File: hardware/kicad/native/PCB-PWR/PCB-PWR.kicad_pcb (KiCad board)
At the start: 4 copper layers, 90 x 60 mm, 60 parts, among them J1 43045-0213, J2 43045-1202, Q1 CSD18540Q5B, U1 LM74700QDBVRQ1, U2 INA226AIDGSR, U3 LMR604403SRAKR, U4 LMR604403SRAKR, U5 TPS7A2018PDBVR

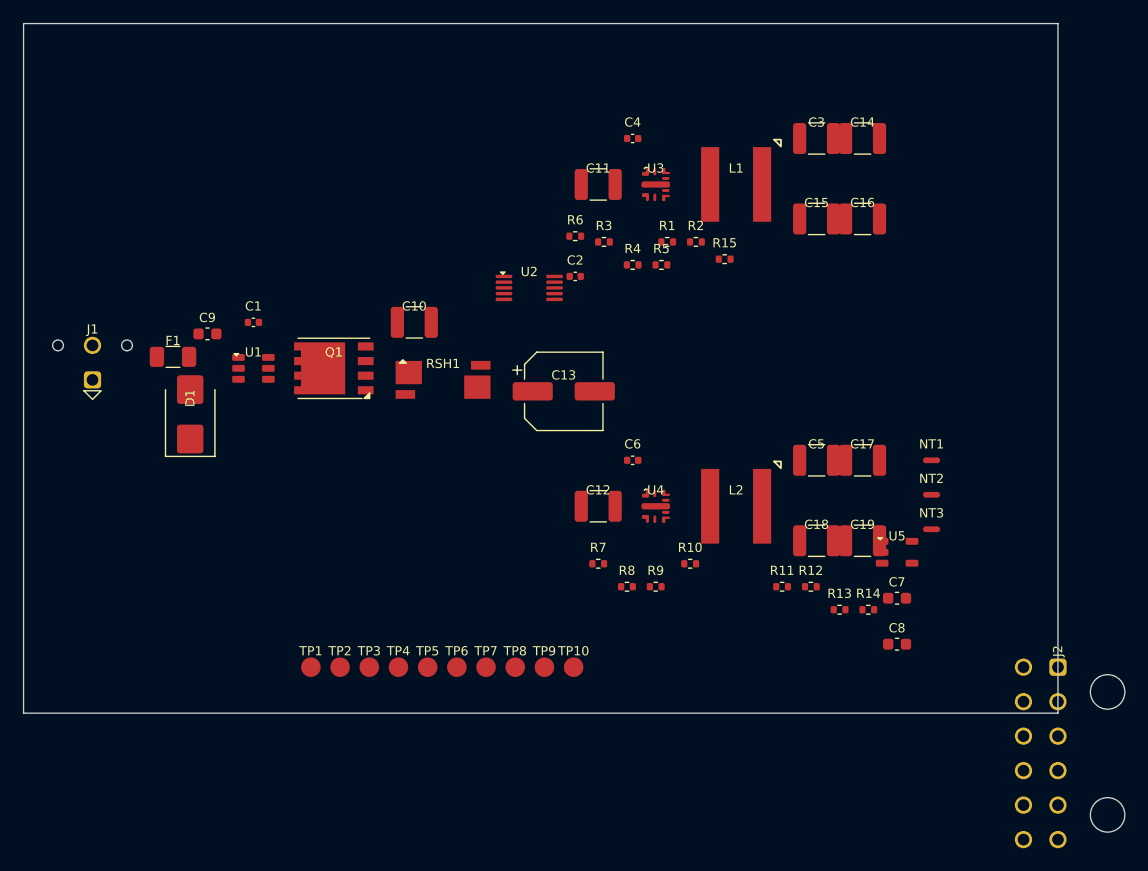
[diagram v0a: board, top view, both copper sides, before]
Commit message: hardware: close PCB-PWR fitted 2D clearance
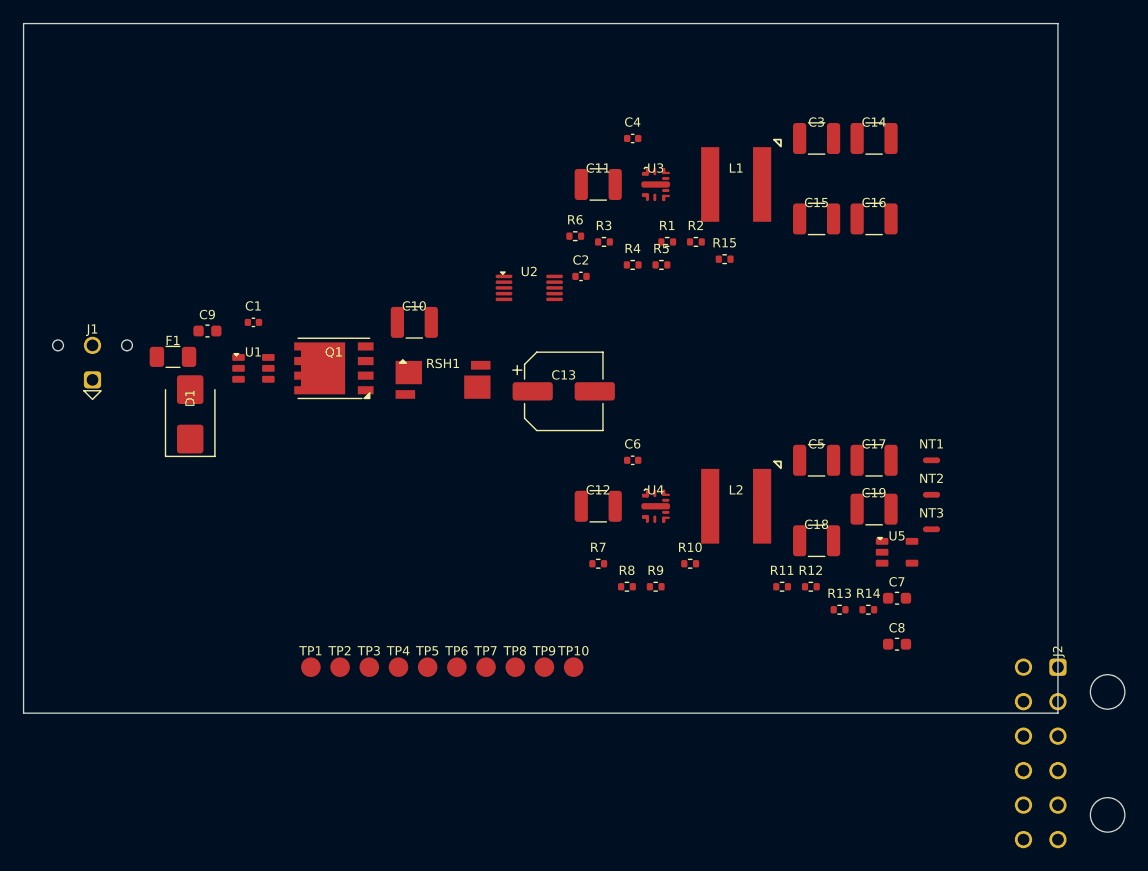
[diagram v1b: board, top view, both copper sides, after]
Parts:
- moved C19 2.93 mm to (74.0, 42.2)
- moved C14 1.00 mm to (74.0, 10.0)
- moved C16 1.00 mm to (74.0, 17.0)
- moved C17 1.00 mm to (74.0, 38.0)
- moved C2 0.50 mm to (48.5, 22.0)
- moved C9 0.25 mm to (16.0, 26.8)
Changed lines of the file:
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@@
 	(footprint "Capacitor_SMD:C_1210_3225Metric"
 		(layer "F.Cu")
-		(at 73 17)
+		(at 74 17)
 		(descr "DIONEA_PCB_PWR_REV_A|population=FITTED|zone=BUCK_3V8|placement=PROVISIONAL_LOAD_STEP_REVIEW_PENDING|authority=PCB_PWR_PASSIVE_AUTHORITY_REV_A.csv")
 		(tags "DIONEA PCB-PWR PROVISIONAL DIM-003 OPEN")
@@
 	(footprint "Capacitor_SMD:C_1210_3225Metric"
 		(layer "F.Cu")
-		(at 73 38)
+		(at 74 38)
 		(descr "DIONEA_PCB_PWR_REV_A|population=FITTED|zone=BUCK_3V3|placement=PROVISIONAL_LOAD_STEP_REVIEW_PENDING|authority=PCB_PWR_PASSIVE_AUTHORITY_REV_A.csv")
 		(tags "DIONEA PCB-PWR PROVISIONAL DIM-003 OPEN")
@@
 	(footprint "Capacitor_SMD:C_0402_1005Metric"
 		(layer "F.Cu")
-		(at 48 22)
+		(at 48.5 22)
 		(descr "DIONEA_PCB_PWR_REV_A|population=FITTED|zone=CURRENT_SENSE|placement=PROVISIONAL_PLACEMENT_REVIEW_PENDING|authority=PCB_PWR_PASSIVE_AUTHORITY_REV_A.csv")
 		(tags "DIONEA PCB-PWR PROVISIONAL DIM-003 OPEN")
@@
 	(footprint "Capacitor_SMD:C_1210_3225Metric"
 		(layer "F.Cu")
-		(at 73 45)
+		(at 74 42.25)
 		(descr "DIONEA_PCB_PWR_REV_A|population=FITTED|zone=BUCK_3V3|placement=PROVISIONAL_LOAD_STEP_REVIEW_PENDING|authority=PCB_PWR_PASSIVE_AUTHORITY_REV_A.csv")
 		(tags "DIONEA PCB-PWR PROVISIONAL DIM-003 OPEN")
@@
 	(footprint "Capacitor_SMD:C_0603_1608Metric"
 		(layer "F.Cu")
-		(at 16 27)
+		(at 16 26.75)
 		(descr "DIONEA_PCB_PWR_REV_A|population=FITTED|zone=INPUT_PROTECTION|placement=PROVISIONAL_HOT_LOOP_REVIEW_PENDING|authority=PCB_PWR_PASSIVE_AUTHORITY_REV_A.csv")
 		(tags "DIONEA PCB-PWR PROVISIONAL DIM-003 OPEN")
@@
 	(footprint "Capacitor_SMD:C_1210_3225Metric"
 		(layer "F.Cu")
-		(at 73 10)
+		(at 74 10)
 		(descr "DIONEA_PCB_PWR_REV_A|population=FITTED|zone=BUCK_3V8|placement=PROVISIONAL_LOAD_STEP_REVIEW_PENDING|authority=PCB_PWR_PASSIVE_AUTHORITY_REV_A.csv")
 		(tags "DIONEA PCB-PWR PROVISIONAL DIM-003 OPEN")

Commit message: hardware: apply PCB-PWR F1 value-only ECO
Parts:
- F1: value 0451005.MRL CANDIDATE -> 0451008.MRL
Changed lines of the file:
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@@
 			)
 		)
-		(property "Value" "0451005.MRL CANDIDATE"
+		(property "Value" "0451008.MRL"
 			(at 0 1.83 0)
 			(layer "F.Fab")

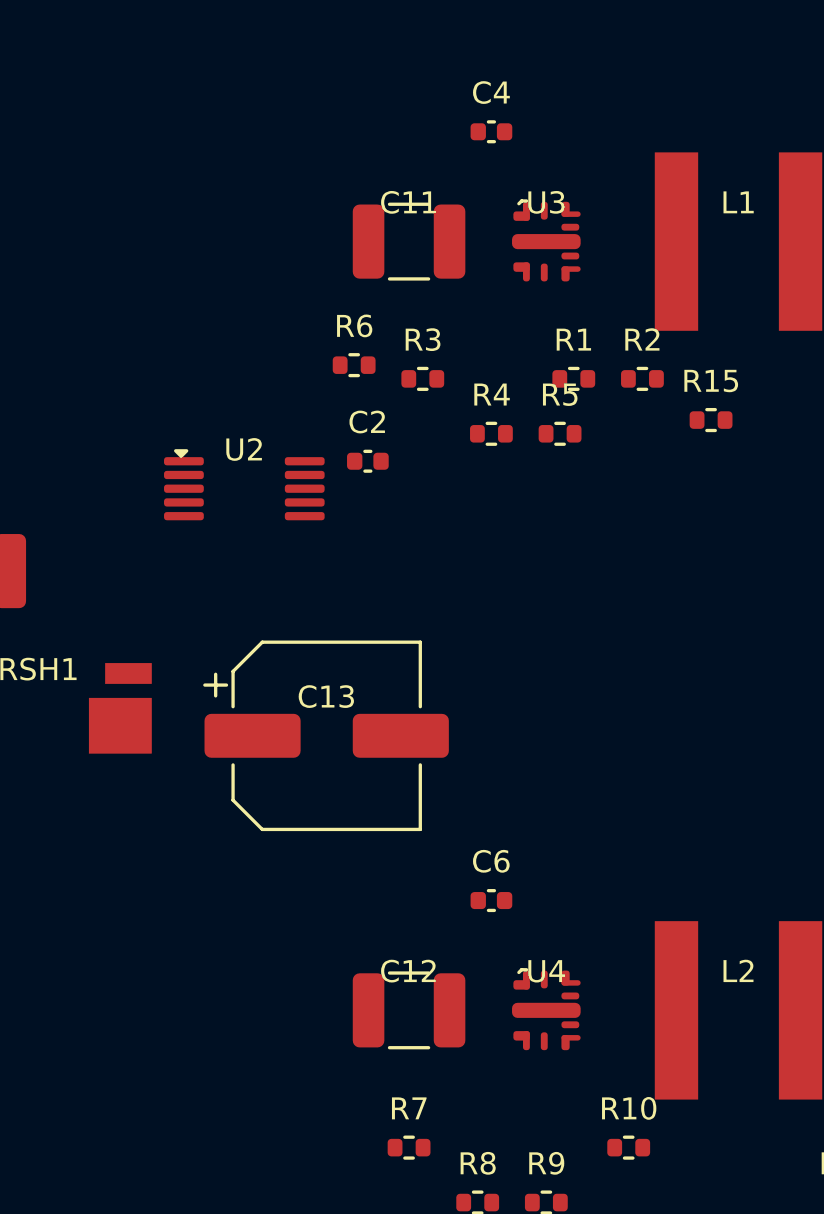
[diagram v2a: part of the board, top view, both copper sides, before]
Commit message: pcb-pwr: add local buck input capacitors
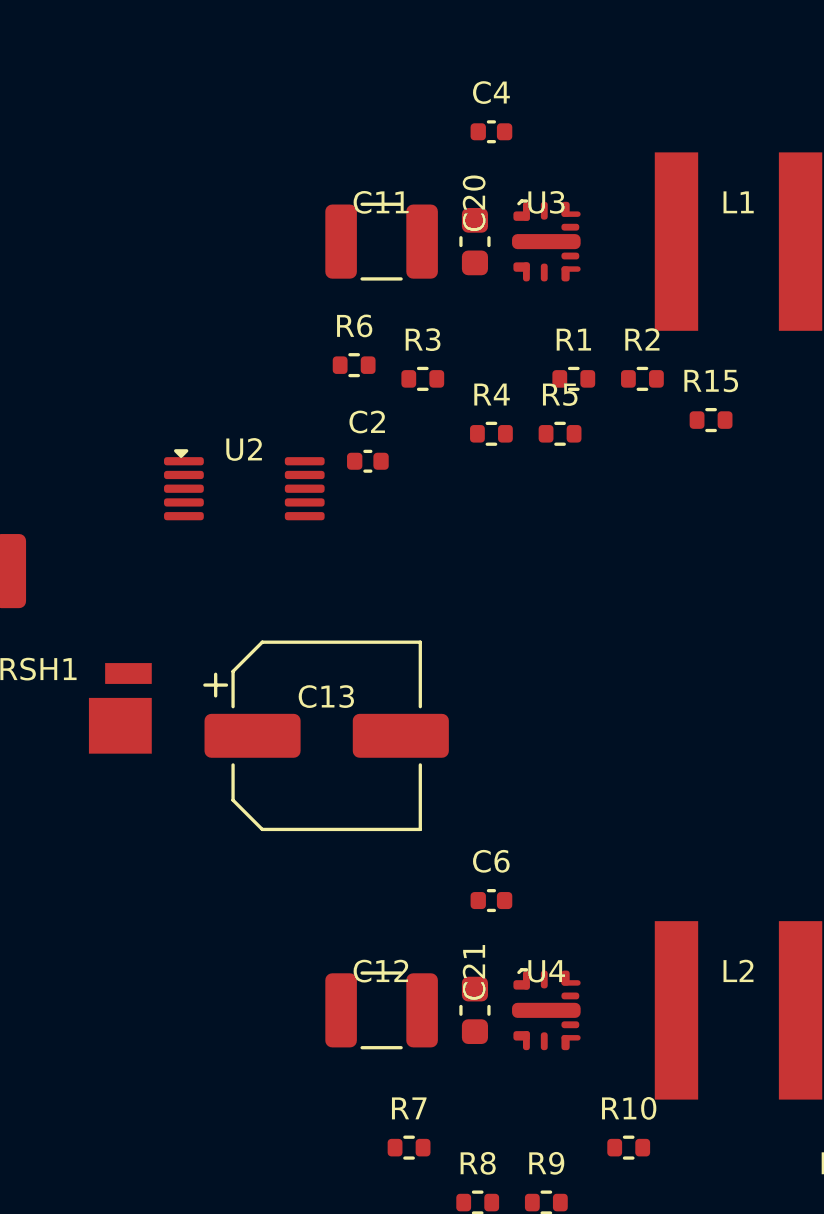
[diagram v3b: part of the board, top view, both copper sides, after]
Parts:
- added C20: 100 nF 50 V X7R CGA3E2X7R1H104K080AA, Capacitor_SMD:C_0603_1608Metric, F.Cu at (52.4, 14.0)
- added C21: 100 nF 50 V X7R CGA3E2X7R1H104K080AA, Capacitor_SMD:C_0603_1608Metric, F.Cu at (52.4, 42.0)
- moved C11 1.00 mm to (49.0, 14.0)
- moved C12 1.00 mm to (49.0, 42.0)

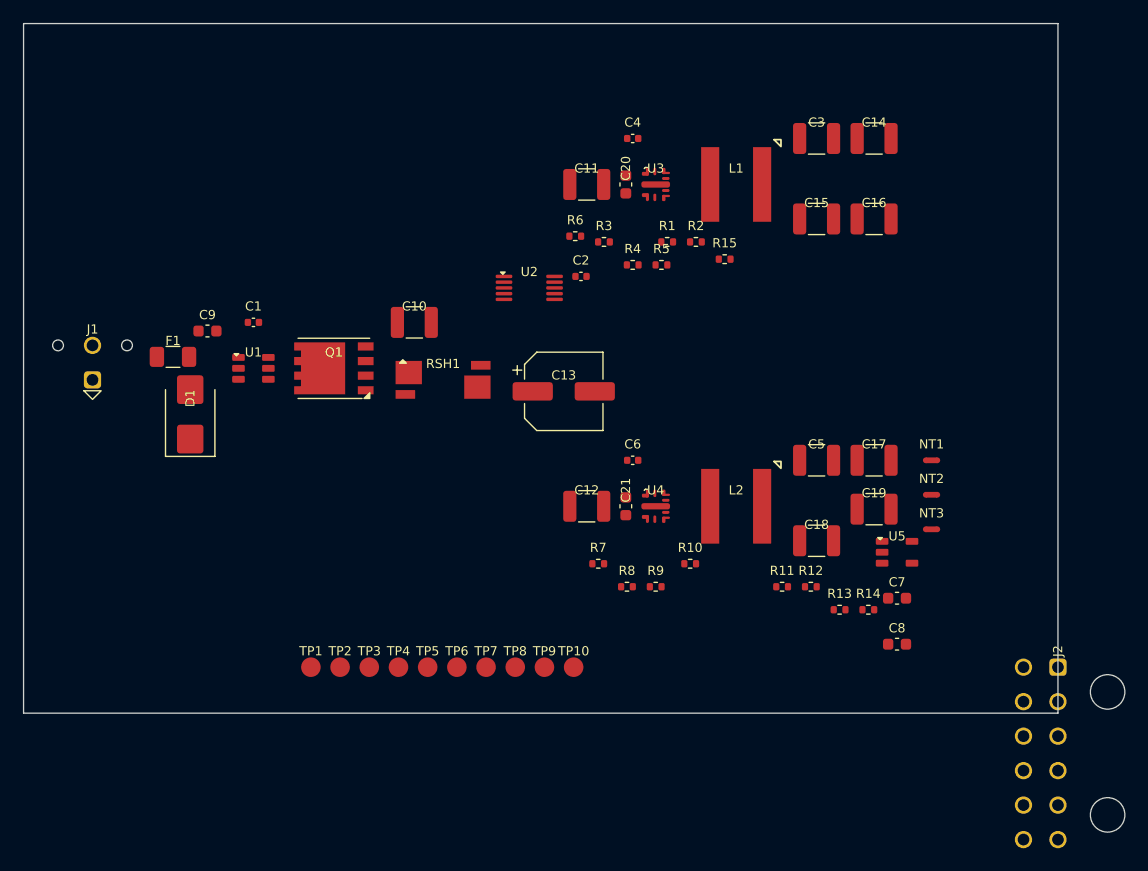
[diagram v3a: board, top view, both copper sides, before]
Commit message: hardware: accept PCB-PWR EVT mechanical authority
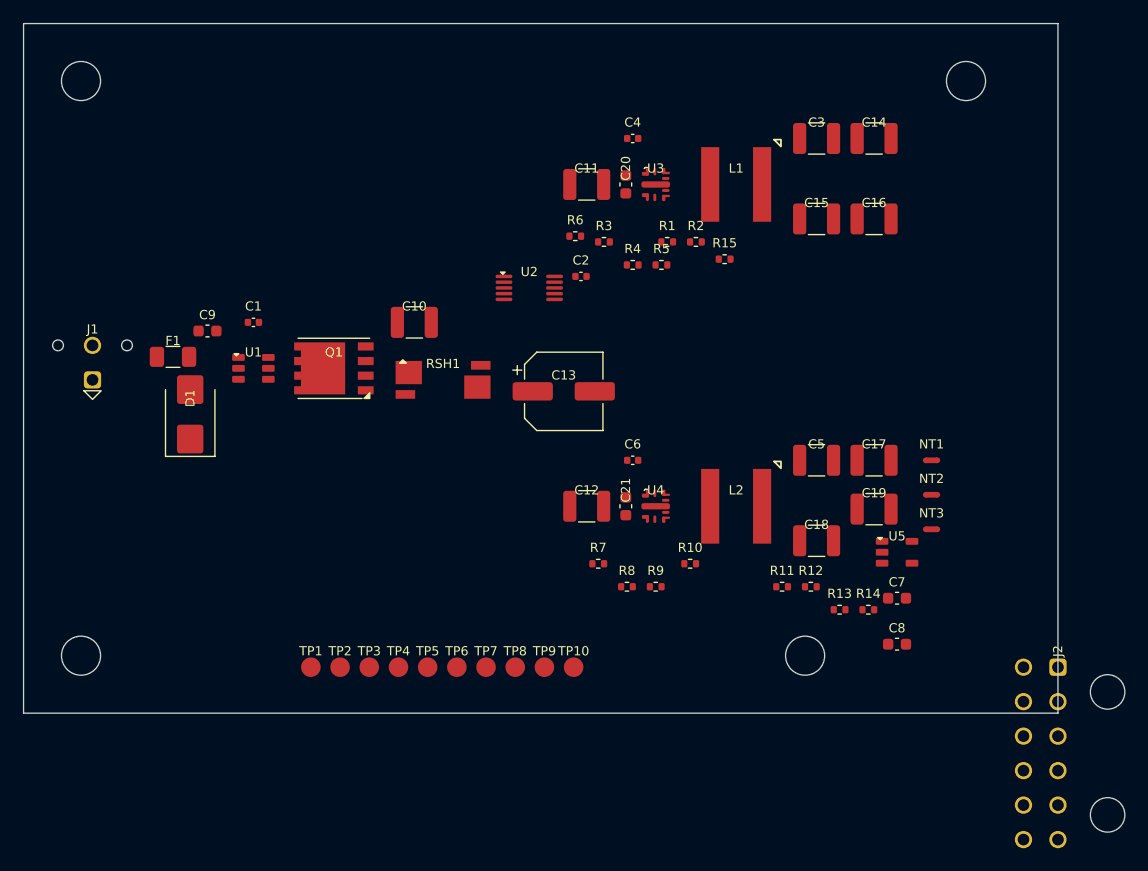
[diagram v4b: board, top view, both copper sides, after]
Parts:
- added H1: M3_CLEARANCE_NPTH_3.4, DioneyaPWR:MountingHole_M3_3.4_EVT, F.Cu at (5.00, 5.00)
- added H2: M3_CLEARANCE_NPTH_3.4, DioneyaPWR:MountingHole_M3_3.4_EVT, F.Cu at (82.0, 5.00)
- added H3: M3_CLEARANCE_NPTH_3.4, DioneyaPWR:MountingHole_M3_3.4_EVT, F.Cu at (68.0, 55.0)
- added H4: M3_CLEARANCE_NPTH_3.4, DioneyaPWR:MountingHole_M3_3.4_EVT, F.Cu at (5.00, 55.0)

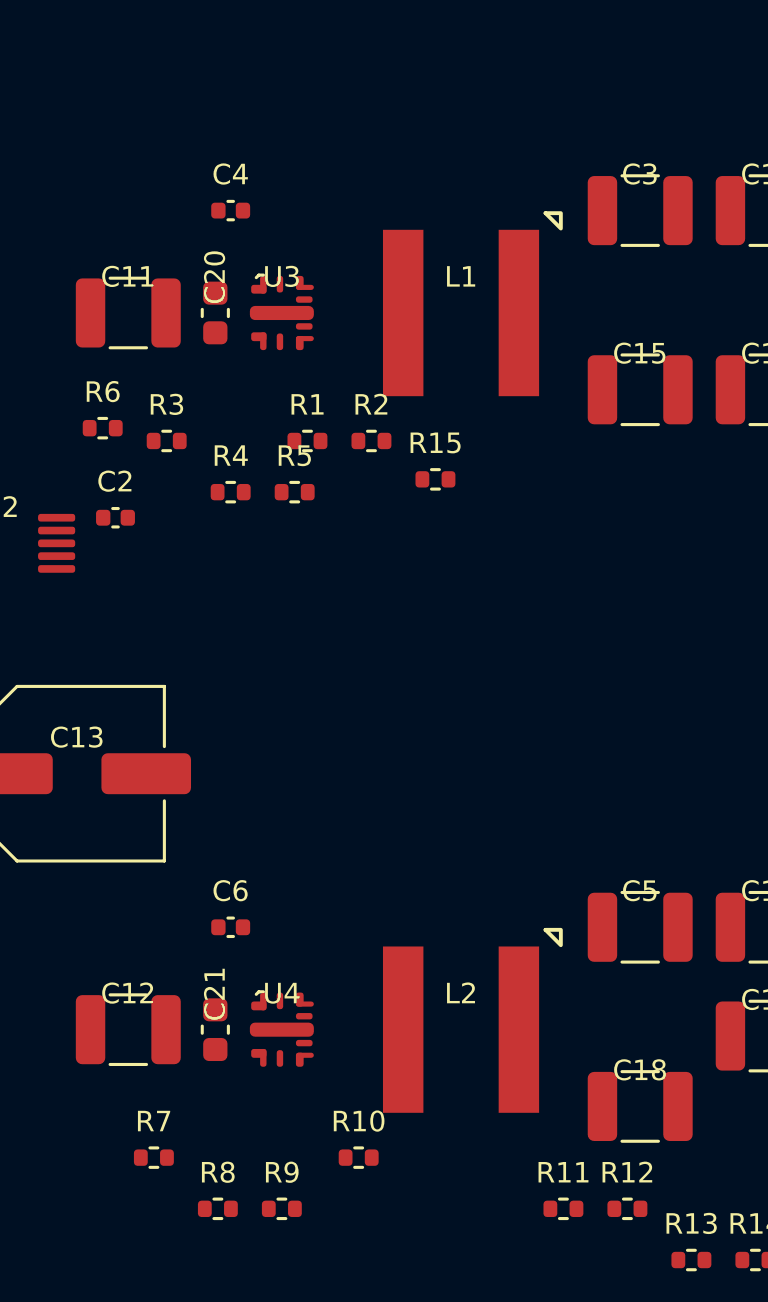
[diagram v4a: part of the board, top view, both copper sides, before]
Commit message: pcb-pwr: apply accepted buck placement ECO-001
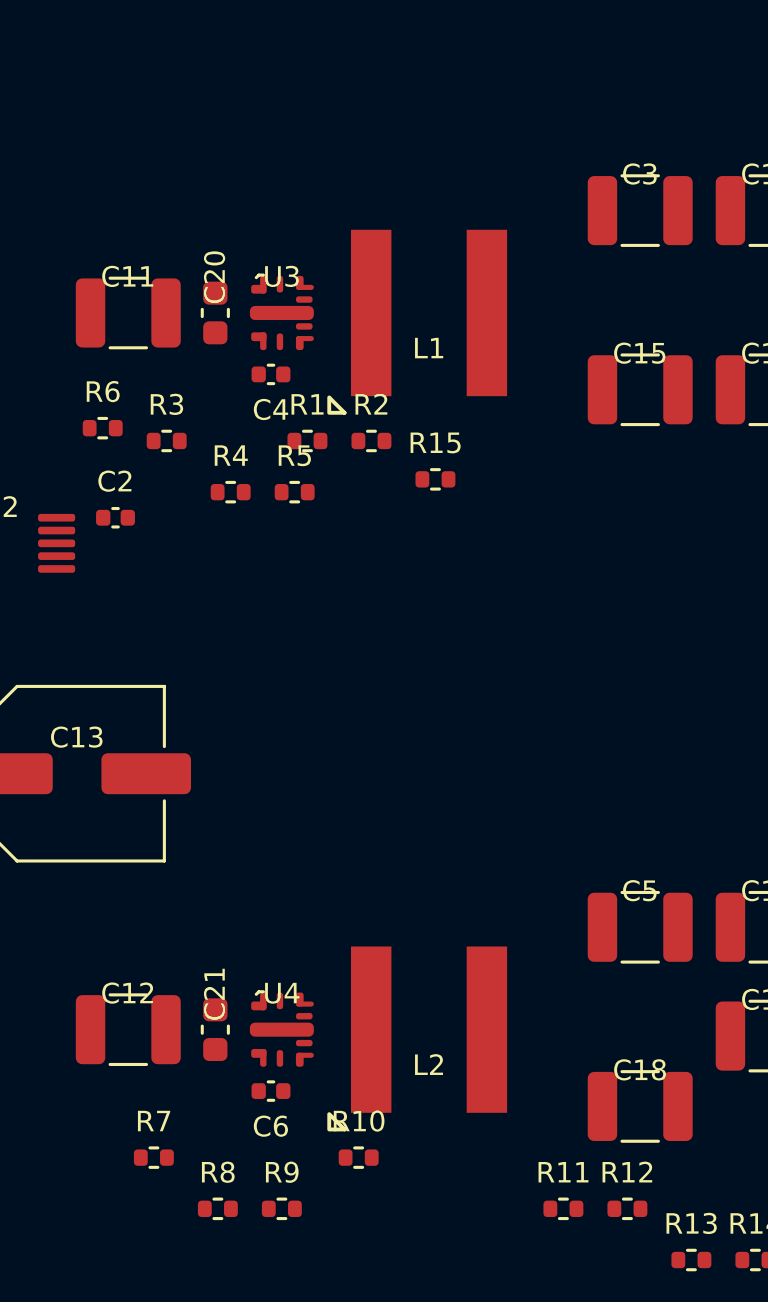
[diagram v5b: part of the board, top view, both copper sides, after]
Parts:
- moved C4 6.59 mm to (54.6, 16.4), turned to 180 degrees
- moved C6 6.59 mm to (54.6, 44.4), turned to 180 degrees
- moved L1 1.25 mm to (60.8, 14.0), turned to 180 degrees
- moved L2 1.25 mm to (60.8, 42.0), turned to 180 degrees
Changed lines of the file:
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@@
 	(footprint "Capacitor_SMD:C_0402_1005Metric"
 		(layer "F.Cu")
-		(at 53 10)
+		(at 54.575 16.4 180)
 		(descr "DIONEA_PCB_PWR_REV_A|population=FITTED|zone=BUCK_3V8|placement=PROVISIONAL_HOT_LOOP_REVIEW_PENDING|authority=PCB_PWR_PASSIVE_AUTHORITY_REV_A.csv")
 		(tags "DIONEA PCB-PWR EVT DIM-003 ACCEPTED NOT FOR MANUFACTURE")
@@
 	(footprint "Capacitor_SMD:C_0402_1005Metric"
 		(layer "F.Cu")
-		(at 53 38)
+		(at 54.575 44.4 180)
 		(descr "DIONEA_PCB_PWR_REV_A|population=FITTED|zone=BUCK_3V3|placement=PROVISIONAL_HOT_LOOP_REVIEW_PENDING|authority=PCB_PWR_PASSIVE_AUTHORITY_REV_A.csv")
 		(tags "DIONEA PCB-PWR EVT DIM-003 ACCEPTED NOT FOR MANUFACTURE")
@@
 	(footprint "DioneyaPWR:Coilcraft_XAL7030_472"
 		(layer "F.Cu")
-		(at 62 42)
+		(at 60.75 42 180)
 		(descr "DIONEA_PCB_PWR_REV_A|population=FITTED|zone=BUCK_3V3|placement=PROVISIONAL_HOT_LOOP_REVIEW_PENDING|authority=PCB_PWR_FOOTPRINT_AUTHORITY_REV_A.md")
 		(tags "DIONEA PCB-PWR EVT DIM-003 ACCEPTED NOT FOR MANUFACTURE")
@@
 	(footprint "DioneyaPWR:Coilcraft_XAL7030_472"
 		(layer "F.Cu")
-		(at 62 14)
+		(at 60.75 14 180)
 		(descr "DIONEA_PCB_PWR_REV_A|population=FITTED|zone=BUCK_3V8|placement=PROVISIONAL_HOT_LOOP_REVIEW_PENDING|authority=PCB_PWR_FOOTPRINT_AUTHORITY_REV_A.md")
 		(tags "DIONEA PCB-PWR EVT DIM-003 ACCEPTED NOT FOR MANUFACTURE")
